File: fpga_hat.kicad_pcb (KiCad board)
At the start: 4 copper layers, 97.8 x 108 mm, 44 parts, among them IC1 ADV7125, IC3 CS4334, U7 Conn_02x32_Odd_Even, U8 Conn_02x32_Odd_Even

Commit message: ...
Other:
- copper layers 4 -> 2

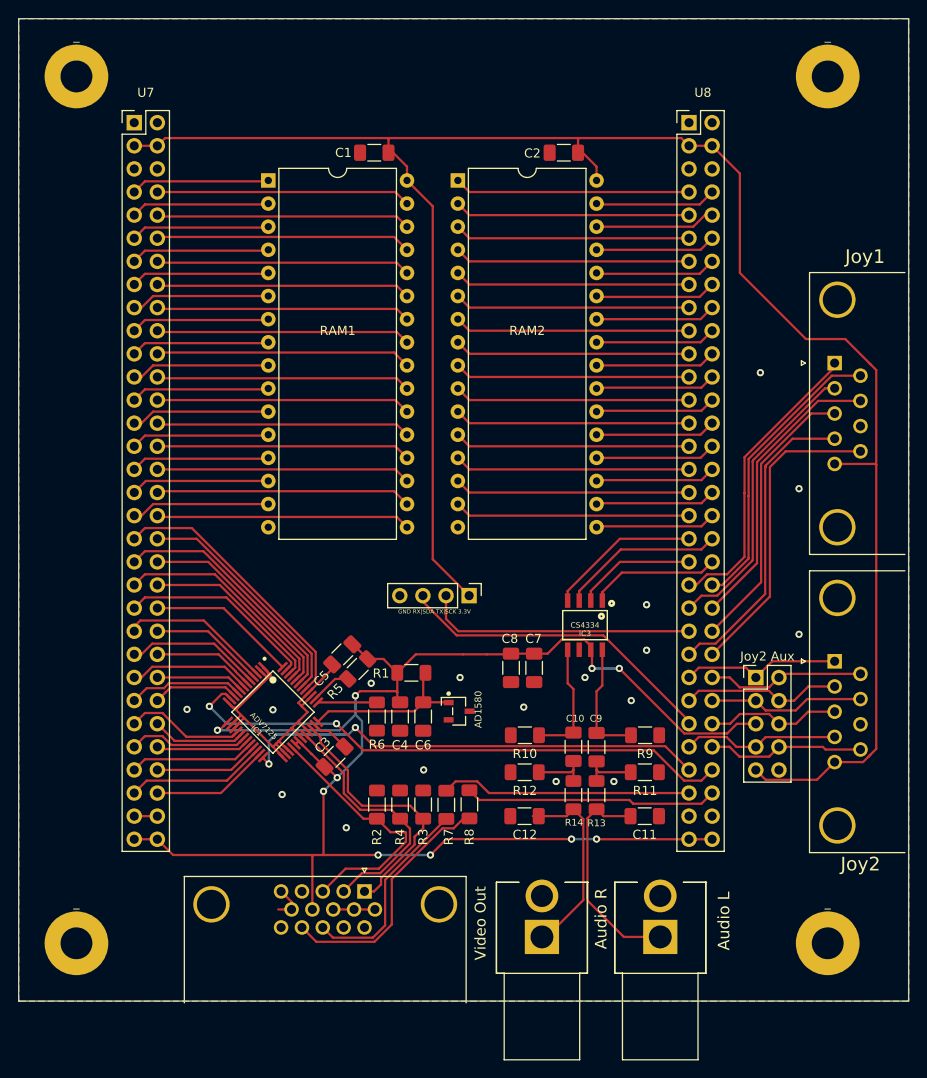
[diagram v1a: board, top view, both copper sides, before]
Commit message: Fixed bad audio routing, added jumper points for running audio trough the vga jack, added missing footprints/symbols
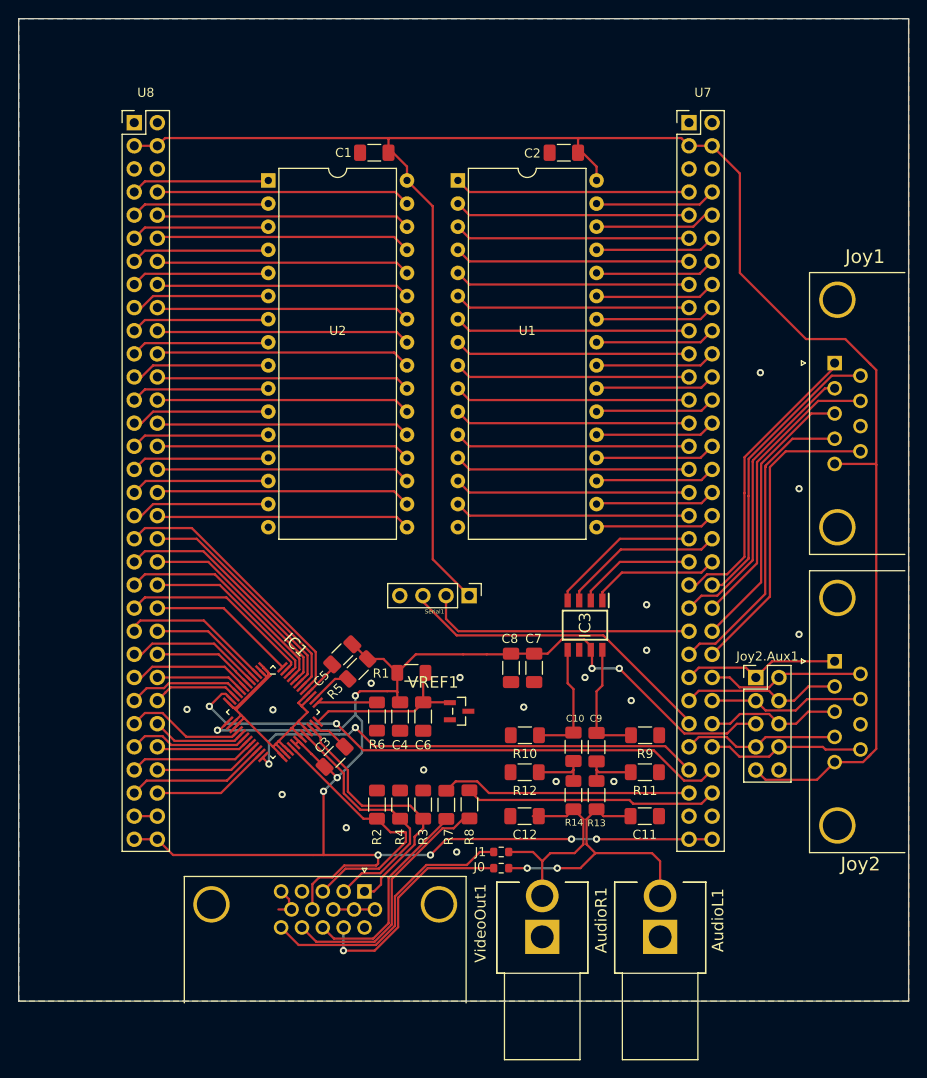
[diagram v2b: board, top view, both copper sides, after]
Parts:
- removed Audio L: Conn_Coaxial, LibraryLoader:KLPX0848A2RG
- removed Audio R: Conn_Coaxial, LibraryLoader:KLPX0848A2RG
- removed _ (x4): MountingHole_3.5mm_Pad, MountingHole:MountingHole_3.5mm_Pad
- added AudioL1: RCA, extralibrary:KLPX0848A2RG, F.Cu at (134.0, 139.0)
- added AudioR1: RCA, extralibrary:KLPX0848A2RG, F.Cu at (121.0, 139.0)
- added J0: 0R, Resistor_SMD:R_0603_1608Metric, F.Cu at (116.5, 131.4)
- added J1: 0R, Resistor_SMD:R_0603_1608Metric, F.Cu at (116.5, 129.7)
- IC1: footprint GithubDownloaded:QFP50P900X900X160-48N -> extralibrary:QFP50P900X900X160-48N
- IC3: footprint GithubDownloaded:SOIC127P600X175-8N -> extralibrary:SOIC127P600X175-8N
- Joy2.Aux1: renamed from Joy2 Aux
- Serial1: renamed from GND RX|SDA TX|SCK 3.3V
- VREF1: renamed from AD1580; footprint GithubDownloaded2:SOT95P237X112-3N -> extralibrary:SOT95P237X112-3N
- VideoOut1: renamed from Video Out
- renumbered RAM2 to U1, RAM1 to U2, U8 to U7, U7 to U8
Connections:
- net Net-(AudioL1-Pad1) renamed AOUTJL
- net Net-(AudioR1-Pad1) renamed AOUTJR
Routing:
- net Net-(J1-Pad2): track 0.00 -> 30.3 mm
- net Net-(J0-Pad2): track 0.00 -> 24.7 mm, vias 0 -> 1
- net +5V: track 177.2 -> 183.0 mm
- net AOUTJL: track 25.7 -> 31.2 mm, vias 0 -> 2
- net AOUTJR: track 22.3 -> 23.1 mm
- net GND: vias 17 -> 18
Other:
- rule pad_to_mask_clearance: 0.05 -> 0

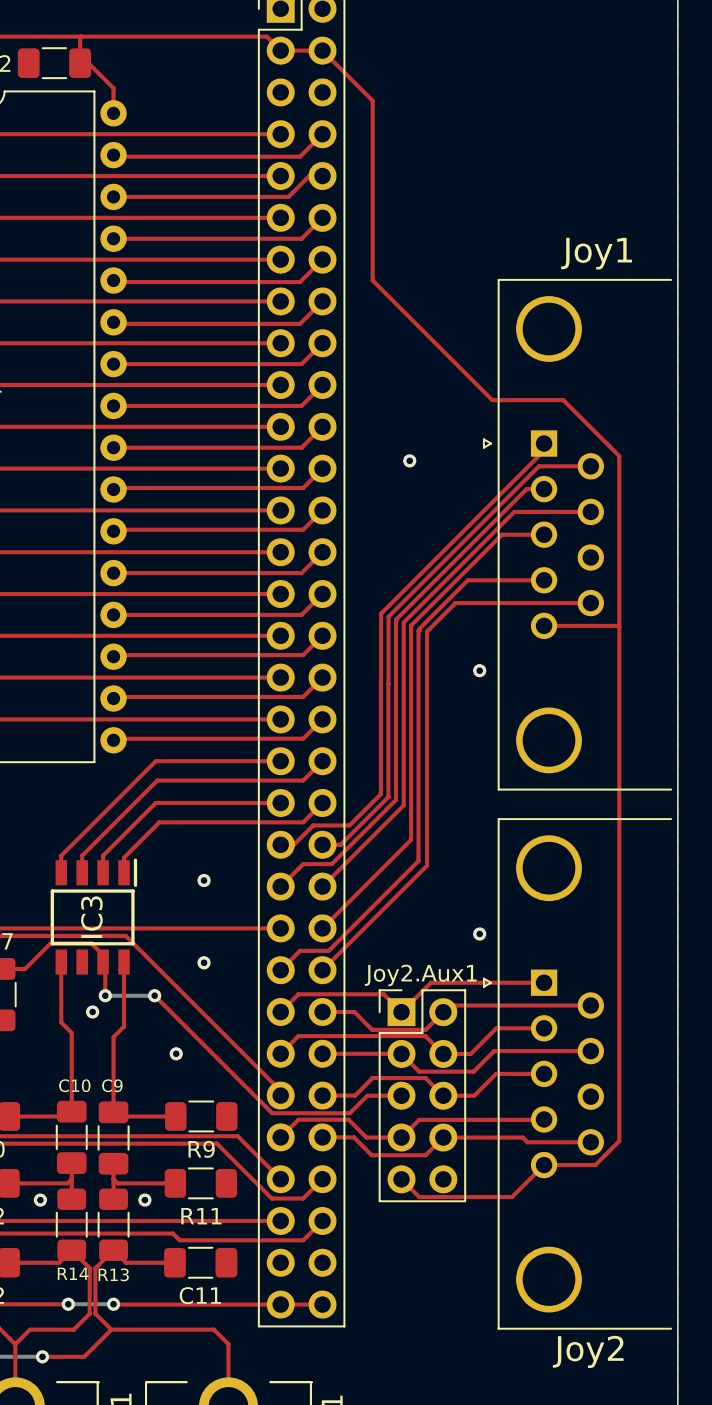
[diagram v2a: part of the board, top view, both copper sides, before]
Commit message: Fixed gamepad port routing
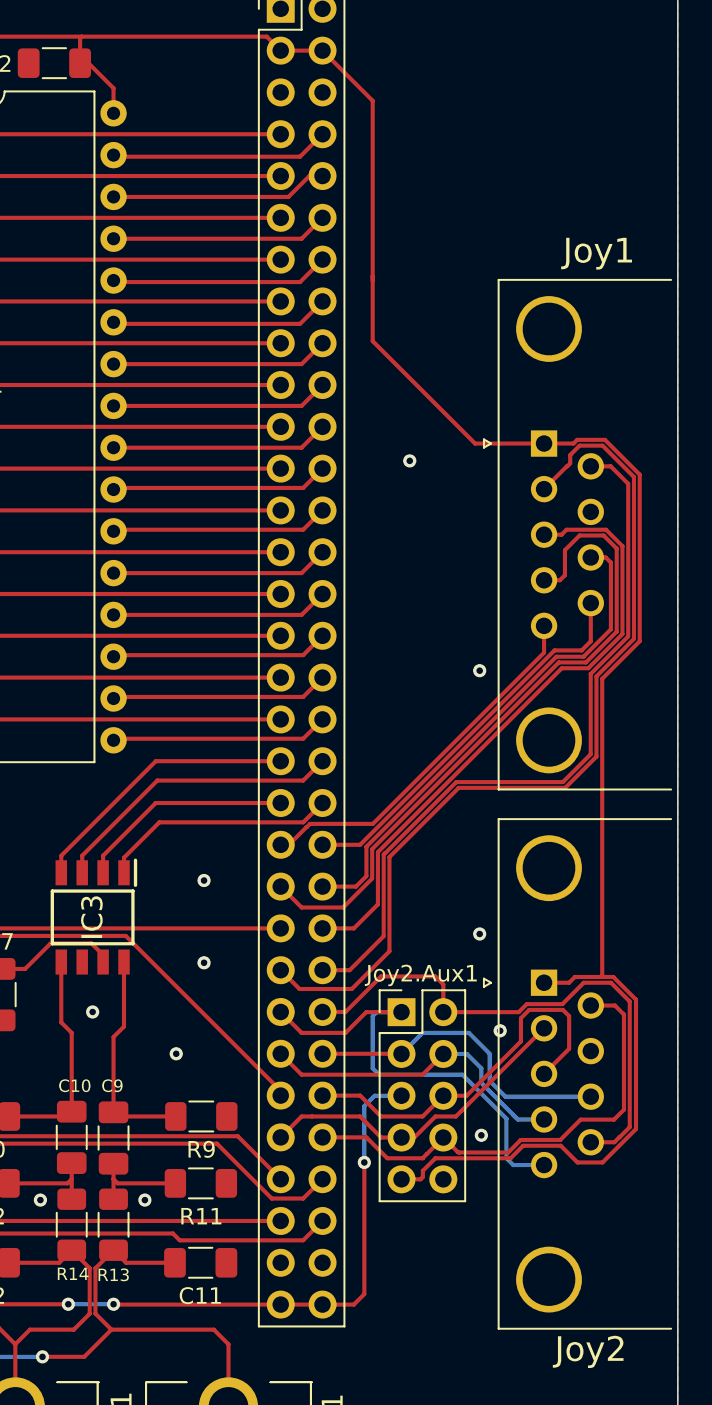
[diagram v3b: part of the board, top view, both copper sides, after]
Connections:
- Joy1 pad 1: /U0 -> +3V3
- Joy1 pad 2: /JD0 -> /JR0
- Joy1 pad 4: /JR0 -> /JD0
- Joy1 pad 5: +3V3 -> /U0
- Joy1 pad 6: /A&B0 -> /S&C0
- Joy1 pad 7: /SEL0 -> GND
- Joy1 pad 8: GND -> /SEL0
- Joy1 pad 9: /S&C0 -> /A&B0
- Joy2 pad 1: /U1 -> +3V3
- Joy2 pad 2: /JD1 -> /JR1
- Joy2 pad 4: /JR1 -> /JD1
- Joy2 pad 5: +3V3 -> /U1
- Joy2 pad 6: /A&B1 -> /S&C1
- Joy2 pad 7: /SEL1 -> GND
- Joy2 pad 8: GND -> /SEL1
- Joy2 pad 9: /S&C1 -> /A&B1
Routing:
- net /JR0: track 34.1 -> 54.4 mm
- net /A&B1: track 17.9 -> 34.6 mm
- net /S&C1: track 18.1 -> 29.3 mm
- net /S&C0: track 33.9 -> 45.0 mm
- net /U0: track 33.4 -> 23.1 mm
- net /U1: track 17.6 -> 27.7 mm
- net /A&B0: track 32.5 -> 23.7 mm
- net /L1: track 14.9 -> 23.3 mm
- net /JD0: track 32.4 -> 40.7 mm
- net /L0: track 31.0 -> 38.1 mm
- net +5V: track 183.0 -> 176.5 mm, vias 10 -> 9
- net +3V3: track 220.7 -> 225.9 mm
- net /JR1: track 17.7 -> 20.0 mm
- net /JD1: track 17.6 -> 19.7 mm
- net /SEL1: track 17.7 -> 19.6 mm
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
